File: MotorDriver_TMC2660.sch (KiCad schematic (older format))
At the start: 16 parts, among them U1 TMC2660

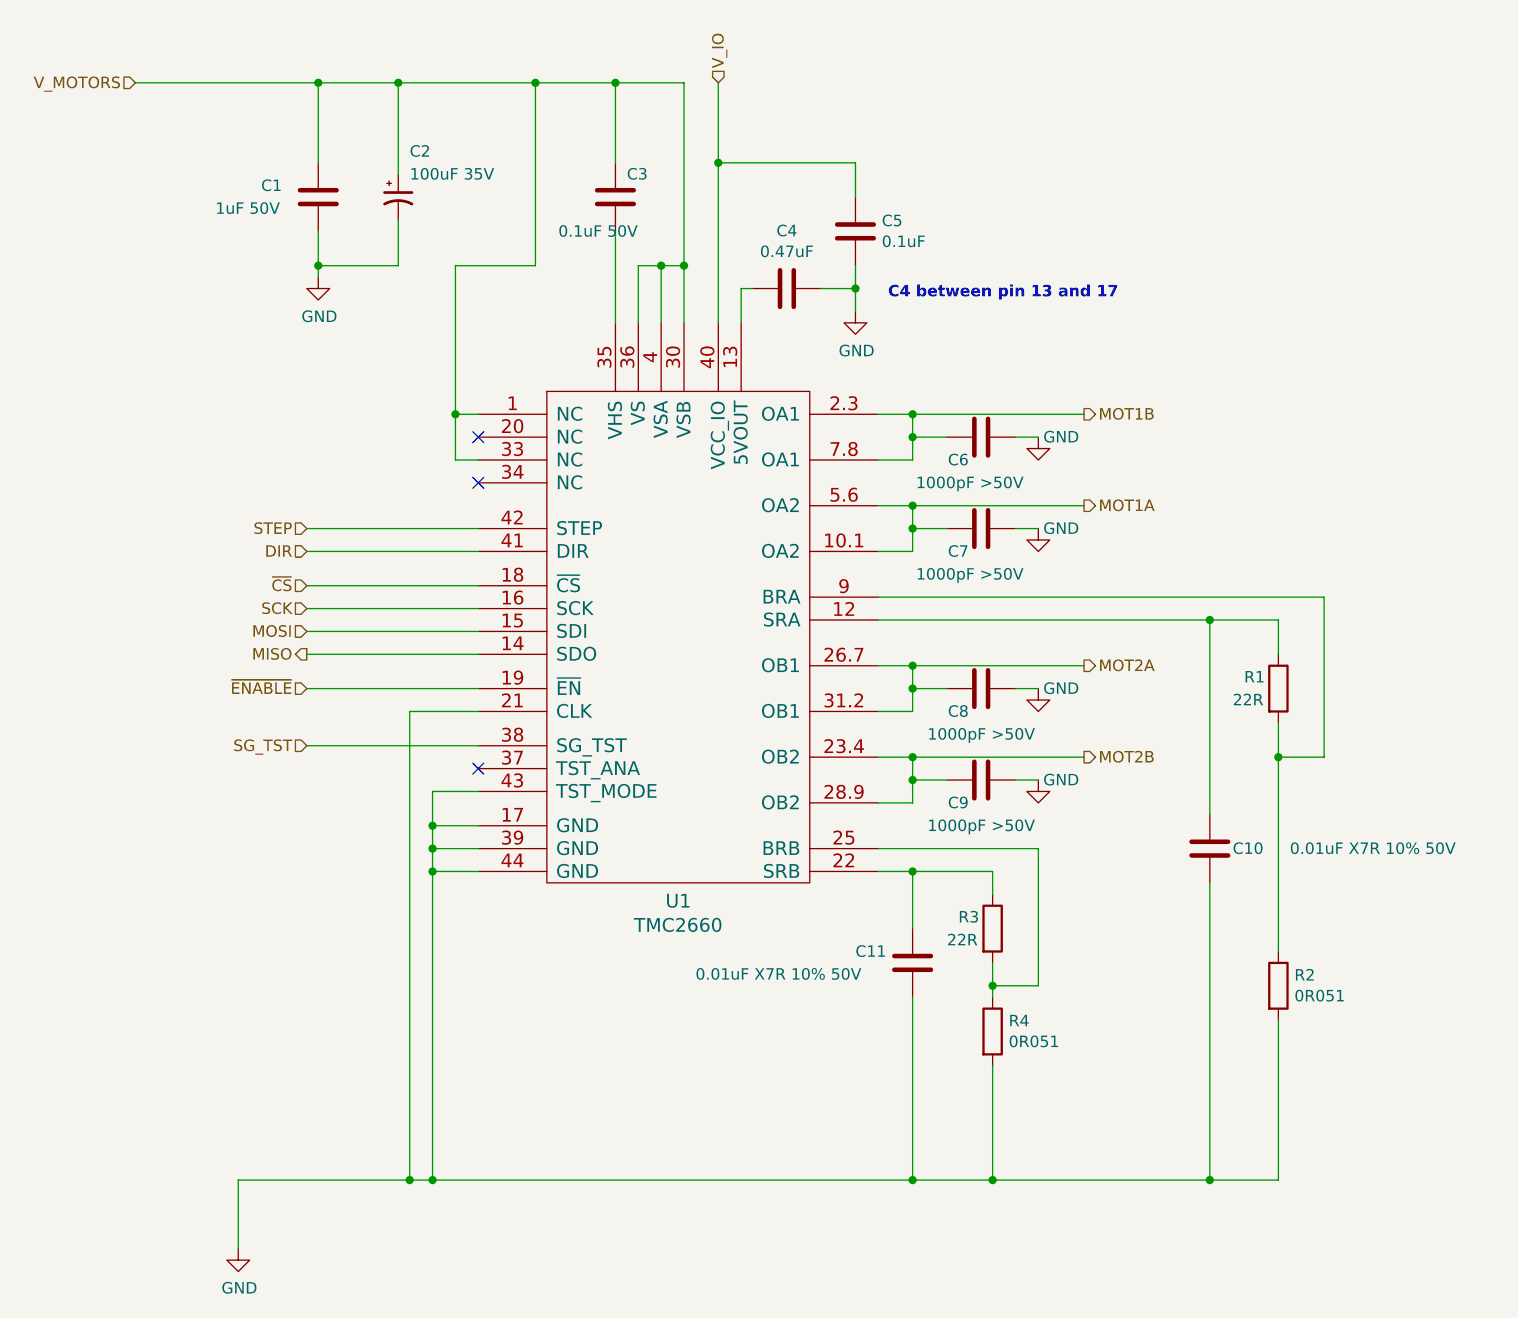
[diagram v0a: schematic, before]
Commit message: Add 3 axis and 2 extruders. Basic thermistor temperature sensing and MOSFET heaters in the extruders.
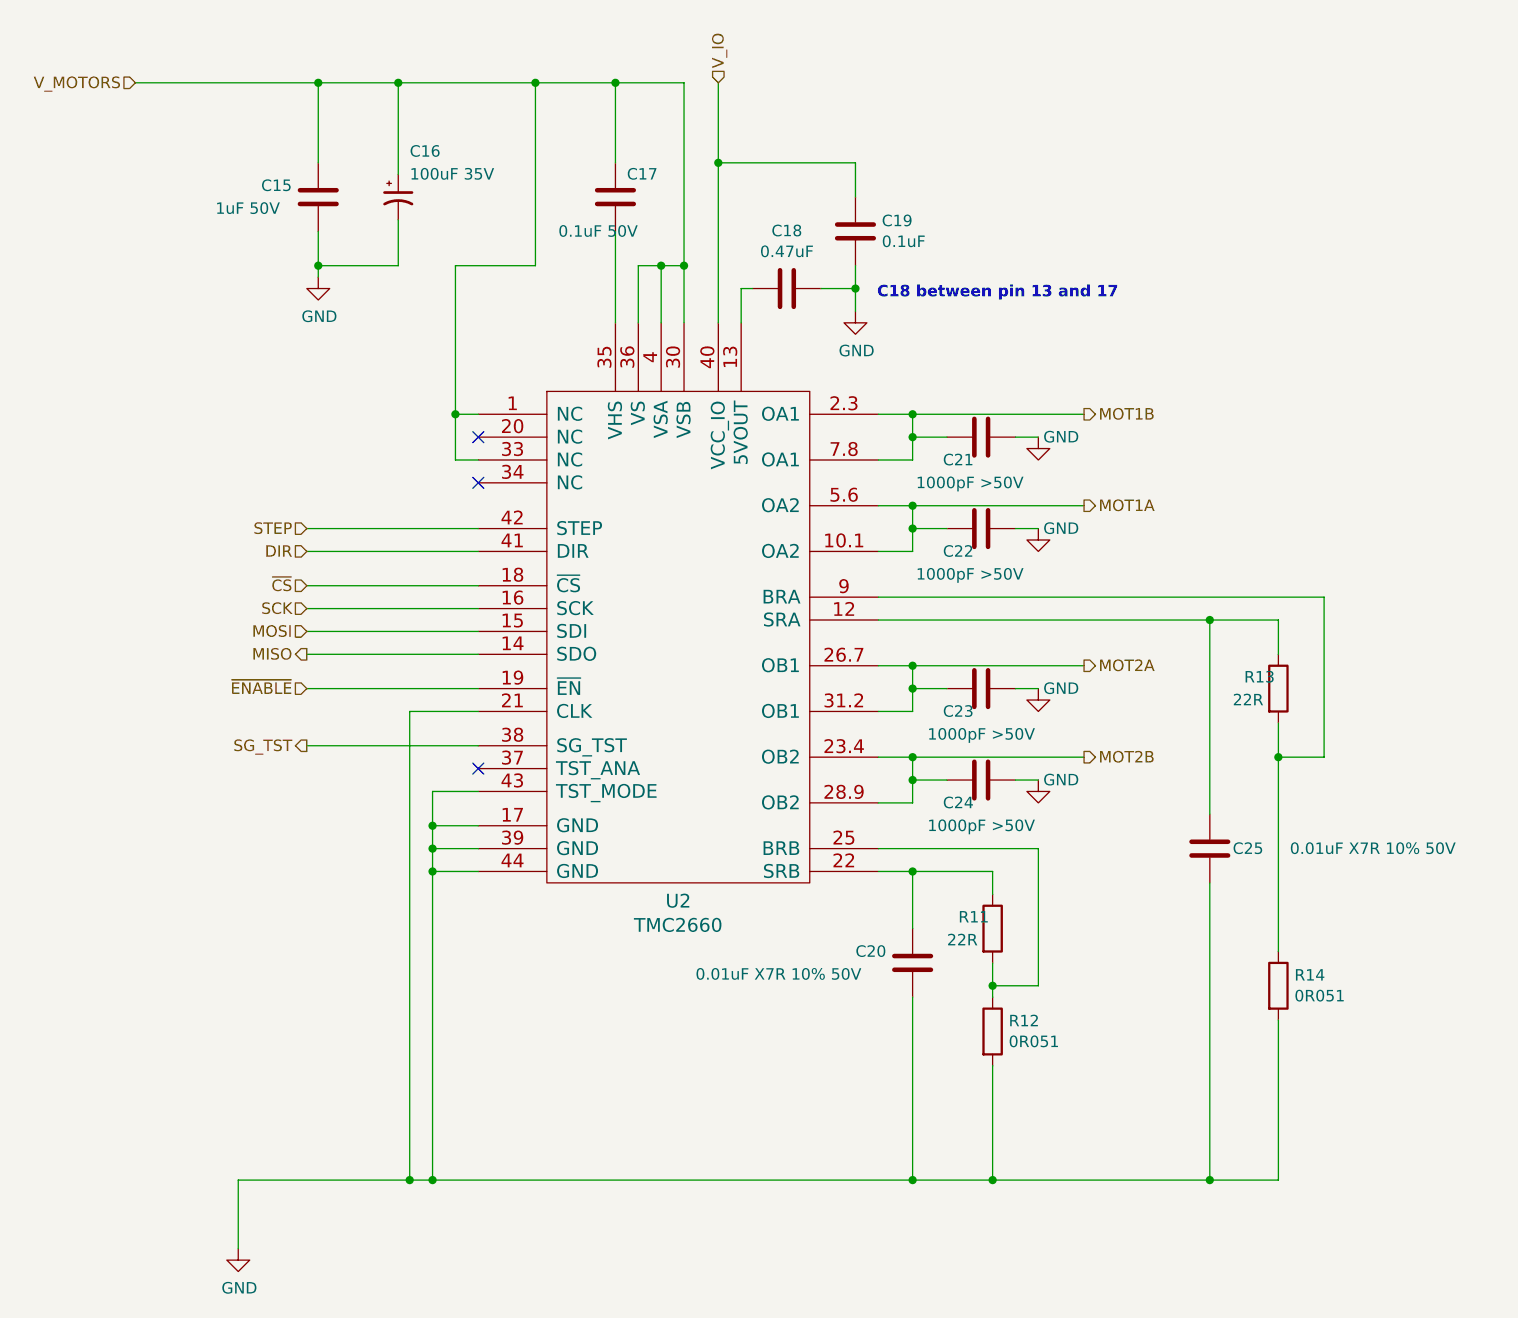
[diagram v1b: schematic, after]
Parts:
- renumbered C9 to C10, C10 to C11, C11 to C6, C6 to C7, C7 to C8, C8 to C9, R3 to R1, R4 to R2, R1 to R3, R2 to R4
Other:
- note added: "C18 between pin 13 and 17"
- note removed: "C4 between pin 13 and 17"

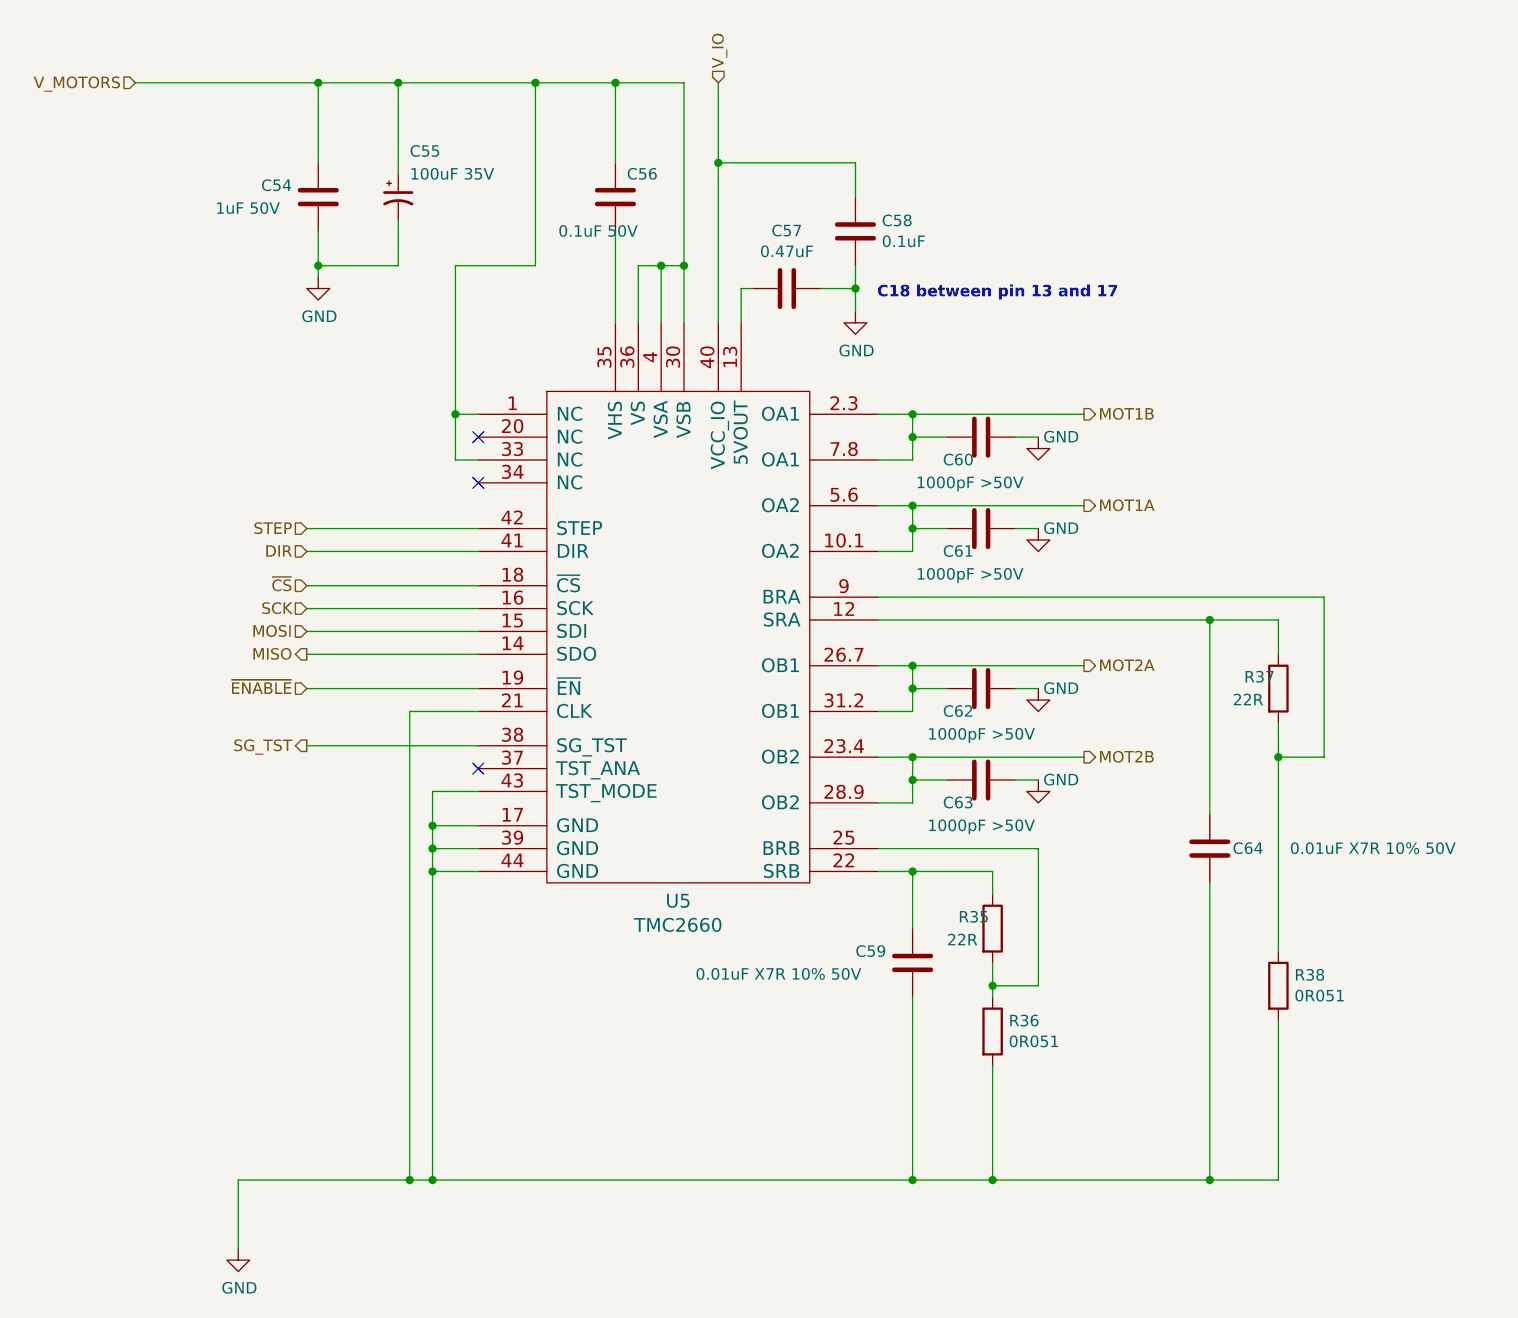
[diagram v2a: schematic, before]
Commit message: Finish the schematics. All pins are assinged to the NUCLEO-64 board.
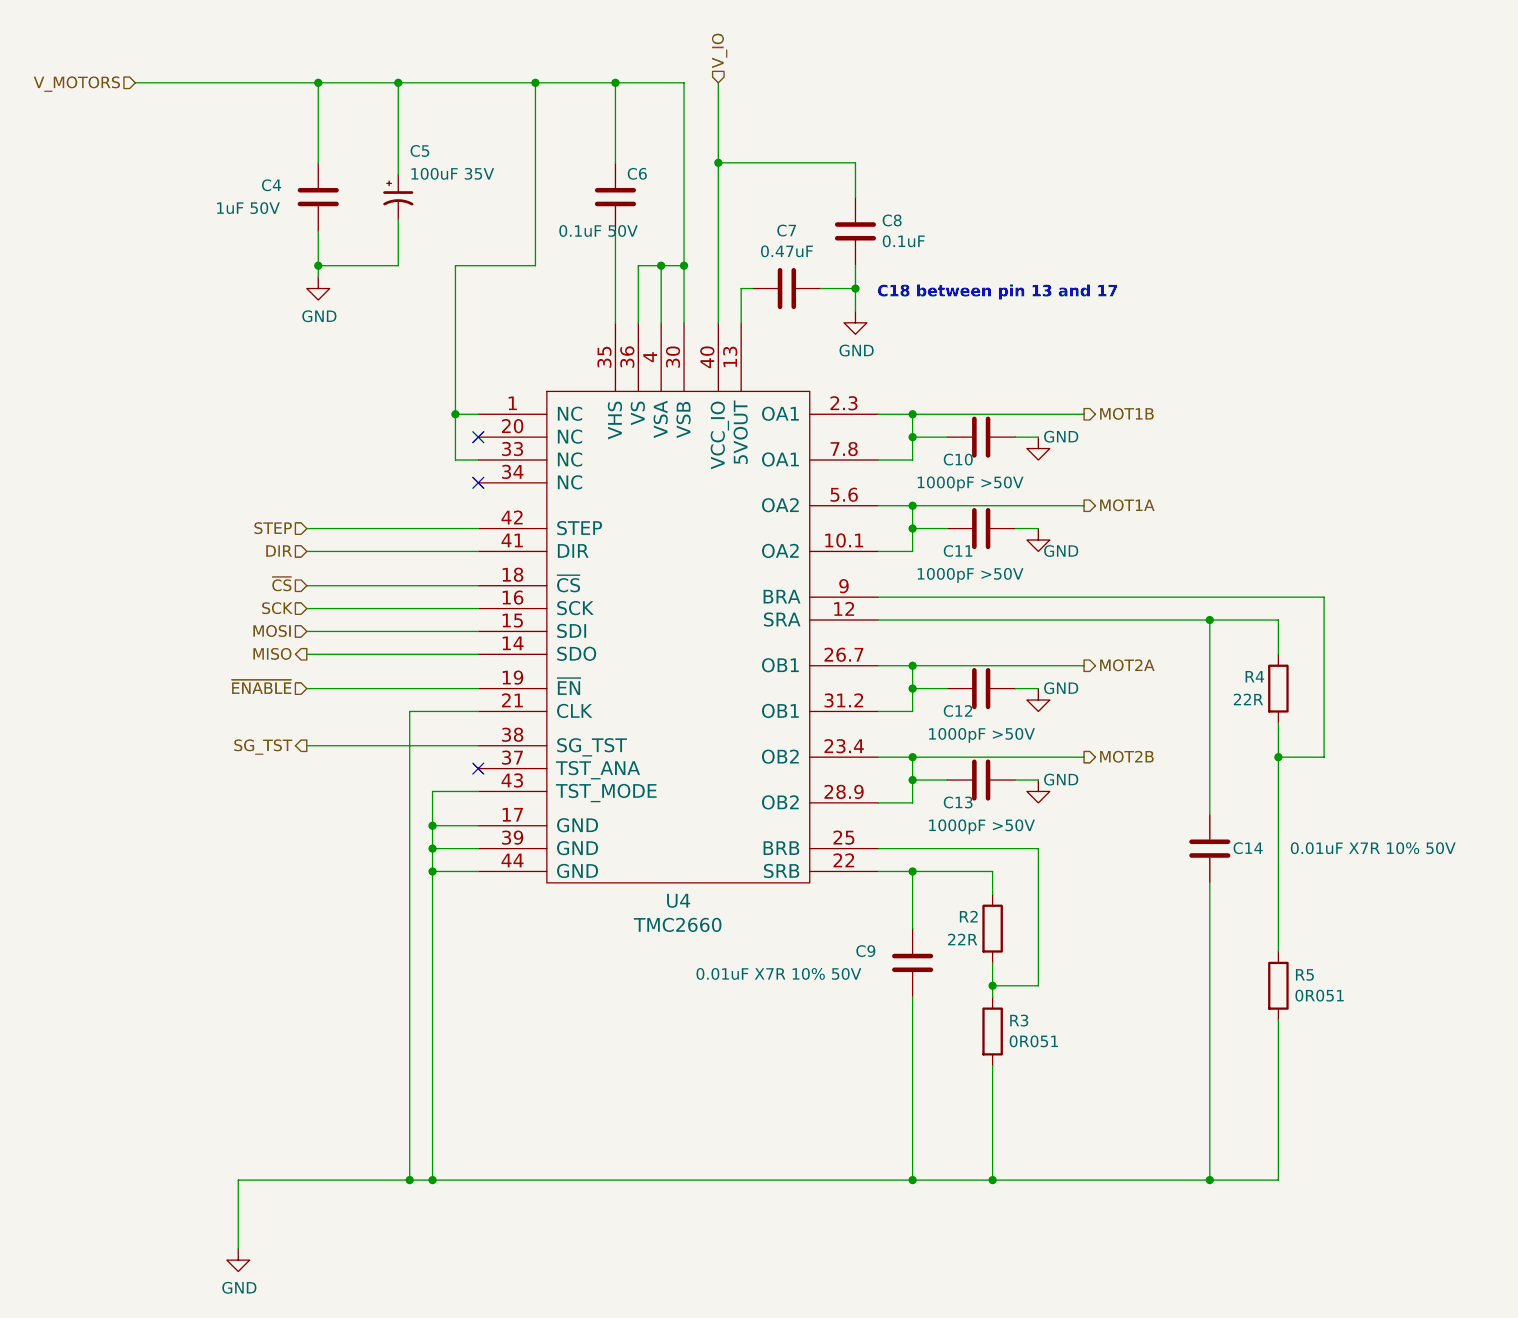
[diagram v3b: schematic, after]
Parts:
- renumbered C7 to C10, C8 to C11, C9 to C12, C10 to C13, C11 to C14, C1 to C4, C2 to C5, C3 to C6, C4 to C7, C5 to C8, C6 to C9, R1 to R2, R2 to R3, R3 to R4, R4 to R5, U1 to U4
